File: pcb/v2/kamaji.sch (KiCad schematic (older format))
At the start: 54 parts, among them J1 RJ10, J2 RJ10, J3 RJ10, J4 RJ10, J5 RJ10, J6 RJ10, J7 USB_B, J8 USB_A, Q1 2N3904, Q2 IRL540N, Q3 IRL540N, SW1 SW_Push, SW2 SW_Push, SW3 SW_Push, U1 ATMEGA32U4-AU, Y1 16MHz

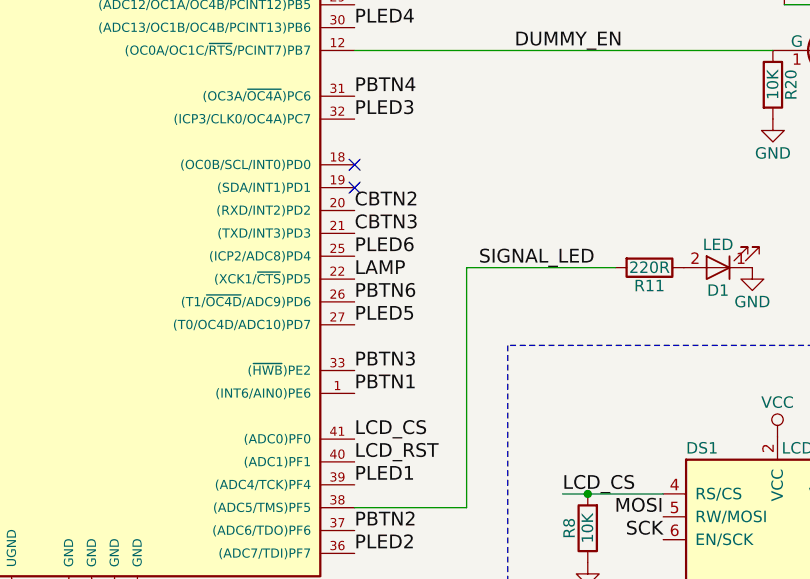
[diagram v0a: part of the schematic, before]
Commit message: pull HWB down
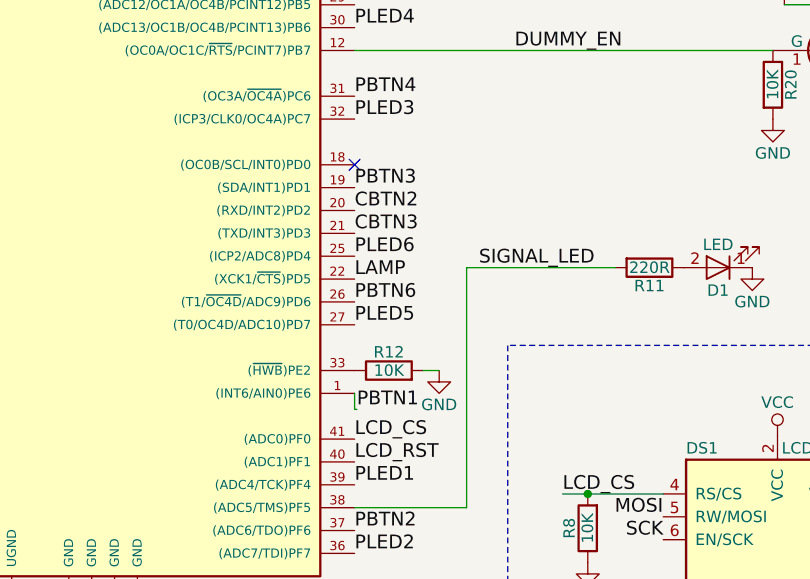
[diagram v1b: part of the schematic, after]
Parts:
- added R12: 10K, Resistors_SMD:R_1206_HandSoldering, symbol R
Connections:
- net GND: now also R12.2
- net PBTN3: now also U1.19 ((SDA/INT1)PD1); no longer U1.33 ((~HWB~)PE2)
- new net: R12.1, U1.33 ((~HWB~)PE2)
- no-connect marks 6 -> 5
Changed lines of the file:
@@
 Text Label 4410 1570 2    60   ~ 0
 RST
-Text Label 3730 3570 0    60   ~ 0
+Text Label 3740 3640 0    60   ~ 0
 PBTN1
 Text Label 3730 3970 0    60   ~ 0
@@
 Text Label 3730 4270 0    60   ~ 0
 PLED2
-Text Label 3730 3470 0    60   ~ 0
+Text Label 3730 2670 0    60   ~ 0
 PBTN3
 Text Label 3730 2770 0    60   ~ 0
@@
 DUMMY-
 NoConn ~ 3730 2570
-NoConn ~ 3730 2670
 $Comp
 L GND #PWR055
@@
 	0    1    1    0
 $EndComp
+$Comp
+L R R12
+U 1 1 5A47814F
+P 3880 3470
+F 0 "R12" V 3960 3470 50  0000 C CNN
+F 1 "10K" V 3880 3470 50  0000 C CNN
+F 2 "Resistors_SMD:R_1206_HandSoldering" V 3810 3470 50  0001 C CNN
+F 3 "" H 3880 3470 50  0001 C CNN
+	1    3880 3470
+	0    -1   -1   0
+$EndComp
+$Comp
+L GND #PWR056
+U 1 1 5A478637
+P 4100 3470
+F 0 "#PWR056" H 4100 3220 50  0001 C CNN
+F 1 "GND" H 4100 3320 50  0000 C CNN
+F 2 "" H 4100 3470 50  0001 C CNN
+F 3 "" H 4100 3470 50  0001 C CNN
+	1    4100 3470
+	1    0    0    -1
+$EndComp
+Wire Wire Line
+	4030 3470 4100 3470
+Wire Wire Line
+	3730 3570 3730 3640
+Wire Wire Line
+	3730 3640 3740 3640
 $EndSCHEMATC

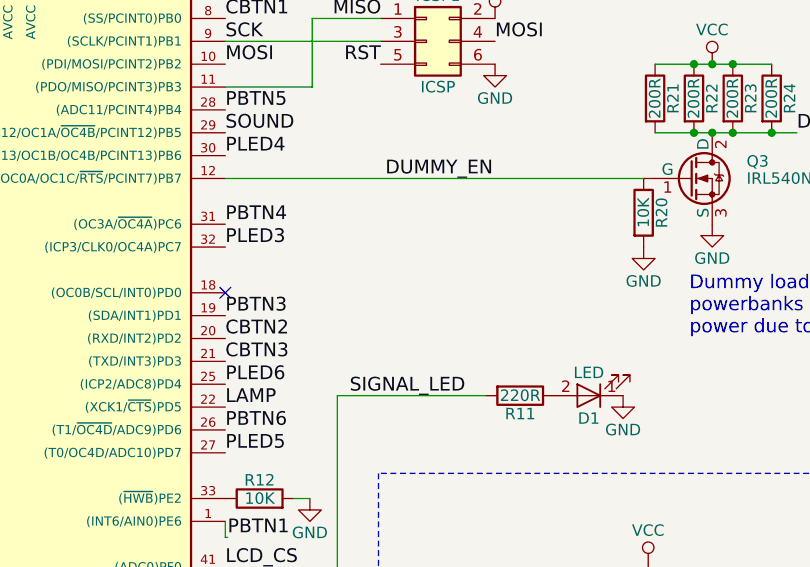
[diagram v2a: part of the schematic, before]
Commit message: xpins for atmega32u4
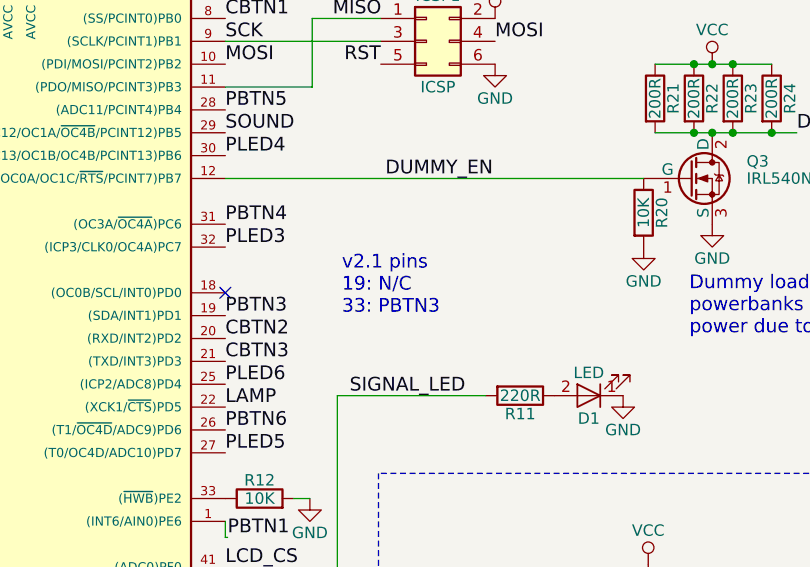
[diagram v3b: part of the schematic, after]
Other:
- note added: "v2.1 pins\n19: N/C\n33: PBTN3"
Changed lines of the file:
@@
 Wire Wire Line
 	3730 3640 3740 3640
+Text Notes 4240 2670 0    60   ~ 0
+v2.1 pins\n19: N/C\n33: PBTN3
 $EndSCHEMATC

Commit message: simplify the PCB a bit
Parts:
- removed R14: 0, Resistors_SMD:R_1206_HandSoldering, symbol R
- removed R25, R26: 10K, Resistors_SMD:R_1206_HandSoldering, symbol R
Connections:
- net GND: now also DS1.15 (PSB)
- net at JP2.2, JP3.2: now also RV2.3
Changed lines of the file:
@@
-$EndComp
-$Comp
-L R R14
-U 1 1 5A3185A6
-P 9510 1730
-F 0 "R14" V 9590 1730 50  0000 C CNN
-F 1 "0" V 9510 1730 50  0000 C CNN
-F 2 "Resistors_SMD:R_1206_HandSoldering" V 9440 1730 50  0001 C CNN
-F 3 "" H 9510 1730 50  0001 C CNN
-	1    9510 1730
-	0    1    1    0
 $EndComp
 $Comp
@@
 	1    0    0    -1
 $EndComp
-$Comp
-L VCC #PWR044
-U 1 1 5A352FEC
-P 6290 4260
-F 0 "#PWR044" H 6290 4110 50  0001 C CNN
-F 1 "VCC" H 6290 4410 50  0000 C CNN
-F 2 "" H 6290 4260 50  0001 C CNN
-F 3 "" H 6290 4260 50  0001 C CNN
-	1    6290 4260
-	1    0    0    -1
-$EndComp
-$Comp
-L R R26
-U 1 1 5A352FF2
-P 6290 4410
-F 0 "R26" V 6210 4410 50  0000 C CNN
-F 1 "10K" V 6290 4410 50  0000 C CNN
-F 2 "Resistors_SMD:R_1206_HandSoldering" V 6220 4410 50  0001 C CNN
-F 3 "" H 6290 4410 50  0001 C CNN
-	1    6290 4410
-	-1   0    0    1
-$EndComp
 NoConn ~ 6080 5010
 $Comp
-L R R25
-U 1 1 5A352FFA
-P 6230 5060
-F 0 "R25" V 6150 5060 50  0000 C CNN
-F 1 "10K" V 6230 5060 50  0000 C CNN
-F 2 "Resistors_SMD:R_1206_HandSoldering" V 6160 5060 50  0001 C CNN
-F 3 "" H 6230 5060 50  0001 C CNN
-	1    6230 5060
-	-1   0    0    1
-$EndComp
-$Comp
-L GND #PWR045
+L GND #PWR044
 U 1 1 5A353001
-P 6230 5210
-F 0 "#PWR045" H 6230 4960 50  0001 C CNN
-F 1 "GND" H 6230 5060 50  0000 C CNN
-F 2 "" H 6230 5210 50  0001 C CNN
-F 3 "" H 6230 5210 50  0001 C CNN
-	1    6230 5210
+P 6230 4910
+F 0 "#PWR044" H 6230 4660 50  0001 C CNN
+F 1 "GND" H 6230 4760 50  0000 C CNN
+F 2 "" H 6230 4910 50  0001 C CNN
+F 3 "" H 6230 4910 50  0001 C CNN
+	1    6230 4910
 	1    0    0    -1
 $EndComp
@@
 ST7920-based LCD display in serial mode
 $Comp
-L GND #PWR046
+L GND #PWR045
 U 1 1 5A35300B
 P 5080 5160
-F 0 "#PWR046" H 5080 4910 50  0001 C CNN
+F 0 "#PWR045" H 5080 4910 50  0001 C CNN
 F 1 "GND" H 5080 5010 50  0000 C CNN
 F 2 "" H 5080 5160 50  0001 C CNN
@@
 	1    0    0    -1
 $EndComp
-Text Label 6480 4560 0    60   ~ 0
+Text Label 6080 4560 0    60   ~ 0
 LCD_RST
 Text Label 4640 4010 0    60   ~ 0
@@
 $EndComp
 $Comp
-L GND #PWR047
+L GND #PWR046
 U 1 1 5A35018A
 P 4880 4980
-F 0 "#PWR047" H 4880 4730 50  0001 C CNN
+F 0 "#PWR046" H 4880 4730 50  0001 C CNN
 F 1 "GND" H 4880 4830 50  0000 C CNN
 F 2 "" H 4880 4980 50  0001 C CNN
@@
 $EndComp
 $Comp
-L VCC #PWR048
+L VCC #PWR047
 U 1 1 5A350190
 P 4880 4680
-F 0 "#PWR048" H 4880 4530 50  0001 C CNN
+F 0 "#PWR047" H 4880 4530 50  0001 C CNN
 F 1 "VCC" H 4880 4830 50  0000 C CNN
 F 2 "" H 4880 4680 50  0001 C CNN
@@
 $EndComp
 $Comp
-L GND #PWR049
+L GND #PWR048
 U 1 1 5A3A8D7F
 P 6470 6970
-F 0 "#PWR049" H 6470 6720 50  0001 C CNN
+F 0 "#PWR048" H 6470 6720 50  0001 C CNN
 F 1 "GND" H 6470 6820 50  0000 C CNN
 F 2 "" H 6470 6970 50  0001 C CNN
@@
 $EndComp
 $Comp
-L GND #PWR050
+L GND #PWR049
 U 1 1 5A3A8D85
 P 6270 6970
-F 0 "#PWR050" H 6270 6720 50  0001 C CNN
+F 0 "#PWR049" H 6270 6720 50  0001 C CNN
 F 1 "GND" H 6270 6820 50  0000 C CNN
 F 2 "" H 6270 6970 50  0001 C CNN
@@
 $EndComp
 $Comp
-L GND #PWR051
+L GND #PWR050
 U 1 1 5A3B984D
 P 1430 4360
-F 0 "#PWR051" H 1430 4110 50  0001 C CNN
+F 0 "#PWR050" H 1430 4110 50  0001 C CNN
 F 1 "GND" H 1430 4210 50  0000 C CNN
 F 2 "" H 1430 4360 50  0001 C CNN
@@
 $EndComp
 $Comp
-L VCC #PWR052
+L VCC #PWR051
 U 1 1 5A3B9853
 P 1430 4060
-F 0 "#PWR052" H 1430 3910 50  0001 C CNN
+F 0 "#PWR051" H 1430 3910 50  0001 C CNN
 F 1 "VCC" H 1430 4210 50  0000 C CNN
 F 2 "" H 1430 4060 50  0001 C CNN
@@
 $EndComp
 $Comp
-L GND #PWR053
+L GND #PWR052
 U 1 1 5A3C2004
 P 5470 3020
-F 0 "#PWR053" H 5470 2770 50  0001 C CNN
+F 0 "#PWR052" H 5470 2770 50  0001 C CNN
 F 1 "GND" H 5470 2870 50  0000 C CNN
 F 2 "" H 5470 3020 50  0001 C CNN
@@
 $EndComp
 $Comp
-L GND #PWR054
+L GND #PWR053
 U 1 1 5A3CD052
 P 10230 1730
-F 0 "#PWR054" H 10230 1480 50  0001 C CNN
+F 0 "#PWR053" H 10230 1480 50  0001 C CNN
 F 1 "GND" H 10230 1580 50  0000 C CNN
 F 2 "" H 10230 1730 50  0001 C CNN
@@
 NoConn ~ 3730 2570
 $Comp
-L GND #PWR055
+L GND #PWR054
 U 1 1 5A3D674E
 P 4750 4310
-F 0 "#PWR055" H 4750 4060 50  0001 C CNN
+F 0 "#PWR054" H 4750 4060 50  0001 C CNN
 F 1 "GND" H 4750 4160 50  0000 C CNN
 F 2 "" H 4750 4310 50  0001 C CNN
@@
 Wire Wire Line
 	4110 1370 4410 1370
-Wire Wire Line
-	9660 1730 9730 1730
-Wire Wire Line
-	9170 1730 9360 1730
 Wire Wire Line
 	1280 1370 1480 1370
@@
 Wire Wire Line
 	6080 4110 6180 4110
-Wire Wire Line
-	6080 4560 6480 4560
-Connection ~ 6290 4560
 Wire Wire Line
 	6080 4910 6230 4910
@@
 $EndComp
 $Comp
-L GND #PWR056
+L GND #PWR055
 U 1 1 5A478637
 P 4100 3470
-F 0 "#PWR056" H 4100 3220 50  0001 C CNN
+F 0 "#PWR055" H 4100 3220 50  0001 C CNN
 F 1 "GND" H 4100 3320 50  0000 C CNN
 F 2 "" H 4100 3470 50  0001 C CNN
@@
 Text Notes 4240 2670 0    60   ~ 0
 v2.1 pins\n19: N/C\n33: PBTN3
+Wire Wire Line
+	9730 1730 9170 1730
 $EndSCHEMATC
